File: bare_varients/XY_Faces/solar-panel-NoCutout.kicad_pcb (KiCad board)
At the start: 4 copper layers, 83 x 98 mm, 32 parts, among them J1 CON-5040500591, J2 Conn_01x01, J3 Conn_01x01, J4 Conn_01x01, J5 Conn_01x01, U1 VEML7700, U2 MCP9808_DFN, U3 DRV2605LDGS

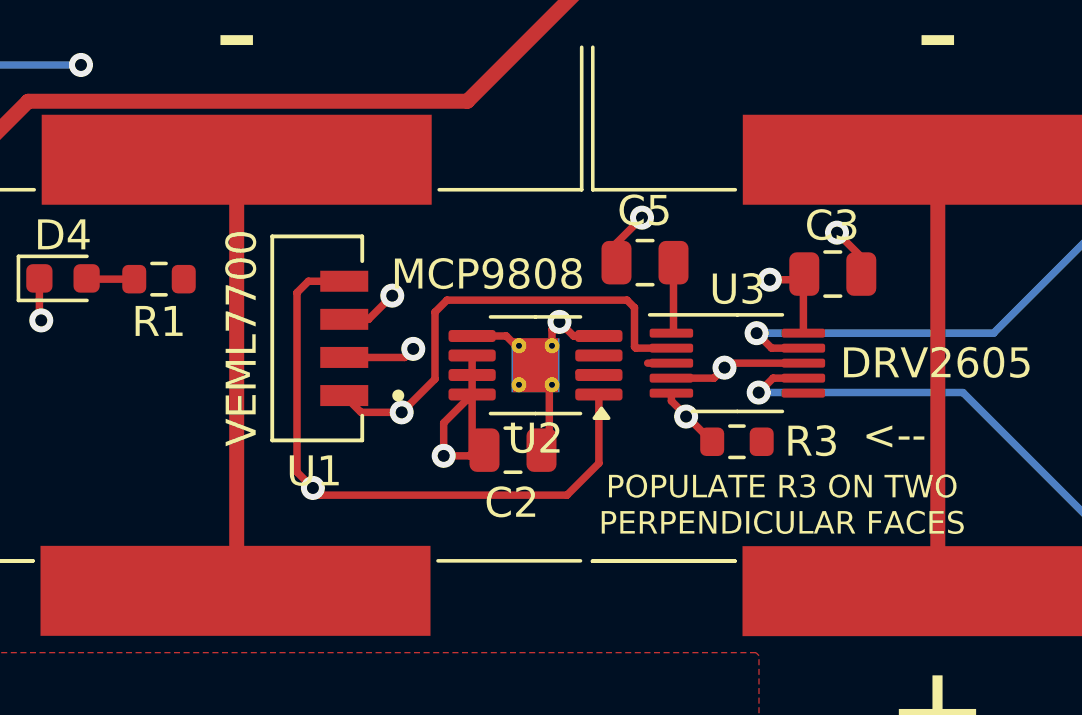
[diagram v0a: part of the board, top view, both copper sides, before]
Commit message: Fixed Broken Traces
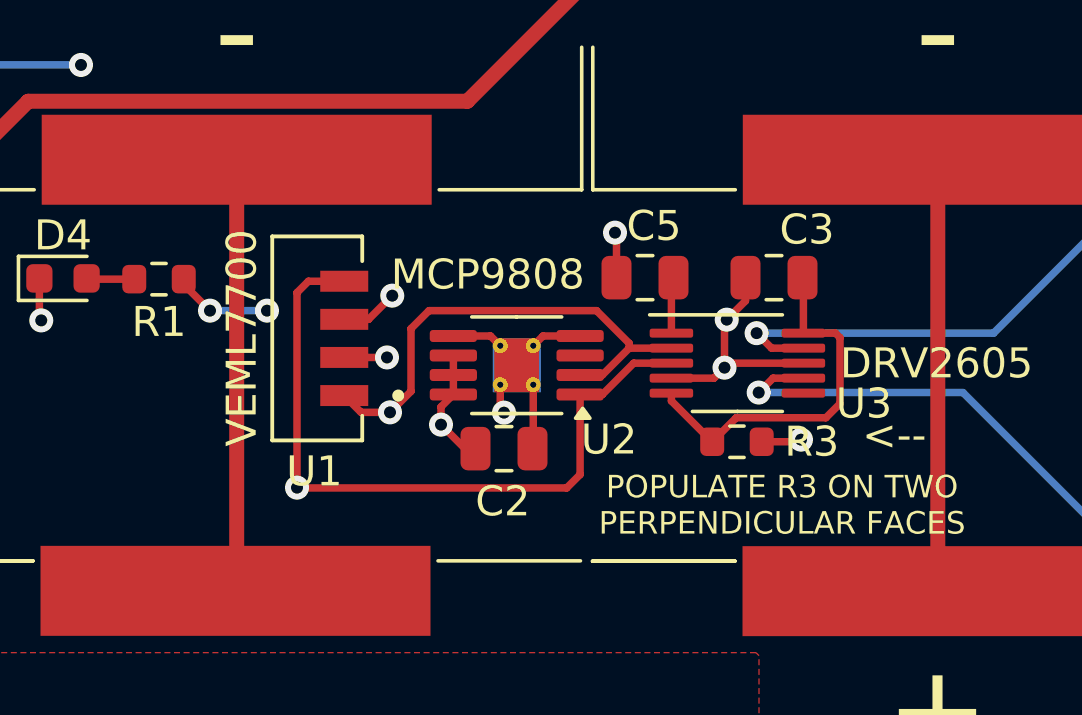
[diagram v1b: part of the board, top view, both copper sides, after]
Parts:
- moved C3 1.96 mm to (162.4, 111.5), turned to 180 degrees
- moved U2 0.62 mm to (153.8, 114.4)
- moved C5 0.50 mm to (158.1, 111.5)
- moved C2 0.30 mm to (153.4, 117.2)
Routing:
- net +3V3: track 28.4 -> 45.2 mm, vias 6 -> 9
- net SDA: track 47.7 -> 49.6 mm
- net Net-(U3-EN): track 11.0 -> 12.4 mm, vias 2 -> 0
- net GND: track 43.2 -> 42.0 mm
